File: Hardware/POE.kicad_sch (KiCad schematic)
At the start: 18 parts, among them J1 Conn_01x07_Male, J10 Conn_01x02_Male, J11 Conn_01x02_Male, J2 Conn_01x04_Male, J3 Conn_01x02_Male, J4 Conn_01x02_Male, J5 Conn_01x02_Male, J6 Conn_01x02_Male, J7 Conn_01x08_Male, J9 QWIIC_Stackable

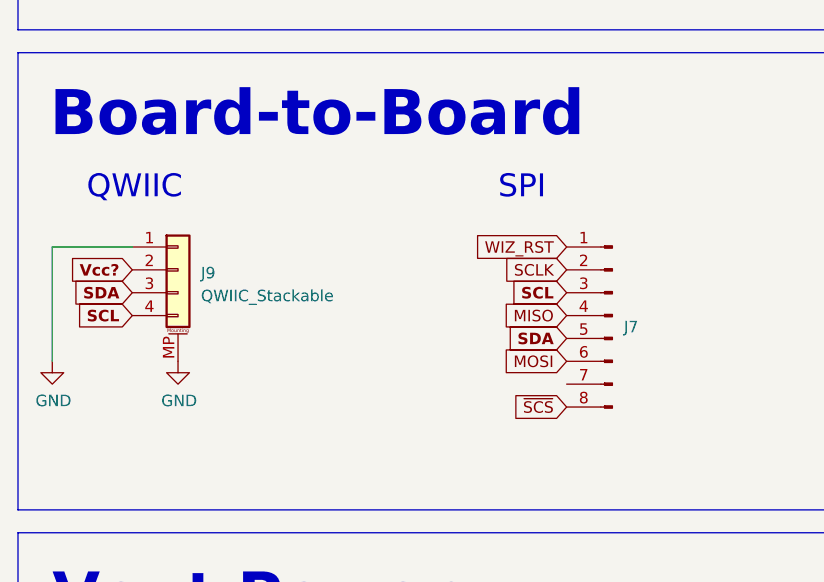
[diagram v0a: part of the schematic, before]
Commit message: Updated POE Board for J7/J9
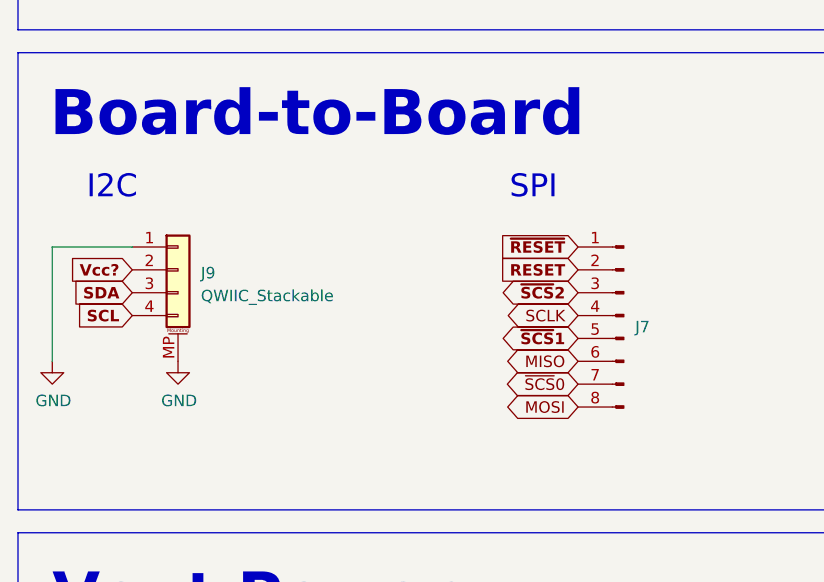
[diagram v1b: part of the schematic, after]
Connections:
- net ~{SCS} is gone; now on net MOSI: J7.8 (Pin_8)
- net MISO: now also J7.6 (Pin_6); no longer J7.4 (Pin_4)
- net MOSI: no longer J7.6 (Pin_6)
- net SCL: no longer J7.3 (Pin_3)
- net SCLK: now also J7.4 (Pin_4); no longer J7.2 (Pin_2)
- net SDA: no longer J7.5 (Pin_5)
- net ~{SCS}0: now reaches J7.7 (Pin_7)
- net WIZ_RST renamed ~{RESET}
- new net RESET: J7.2 (Pin_2)
- new net ~{SCS}1: J7.5 (Pin_5)
- new net ~{SCS}2: J7.3 (Pin_3)
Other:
- note added: "I2C"
- note removed: "QWIIC"
- moved on the sheet: J7
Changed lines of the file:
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@@
   (title_block
     (title "POE")
-    (rev "0.0.0")
+    (rev "0.2.0")
     (company "The Nerd Mage")
     (comment 2 "With help from Austins_Creations")
@@
     (effects (font (size 5 5) (thickness 1) bold) (justify left bottom))
   )
-  (text "QWIIC" (at 21.59 72.39 0)
+  (text "I2C" (at 21.59 72.39 0)
     (effects (font (size 2.54 2.54)) (justify left bottom))
   )
@@
     (effects (font (size 5 5) (thickness 1) bold) (justify left bottom))
   )
-  (text "SPI" (at 67.31 72.39 0)
+  (text "SPI" (at 68.58 72.39 0)
     (effects (font (size 2.54 2.54)) (justify left bottom))
   )
@@
     )
   )
+  (global_label "~{SCS}1" (shape bidirectional) (at 76.2 87.63 180) (fields_autoplaced)
+    (effects (font (size 1.27 1.27) (thickness 0.254) bold) (justify right))
+    (property "Intersheet References" "${INTERSHEET_REFS}" (id 0) (at 68.6979 87.503 0)
+      (effects (font (size 1.27 1.27) (thickness 0.254) bold) (justify right) hide)
+    )
+  )
   (global_label "Vout" (shape input) (at 229.87 143.51 180) (fields_autoplaced)
     (effects (font (size 1.27 1.27)) (justify right))
@@
     )
   )
-  (global_label "MISO" (shape input) (at 74.93 85.09 180) (fields_autoplaced)
-    (effects (font (size 1.27 1.27)) (justify right))
-    (property "Intersheet References" "${INTERSHEET_REFS}" (id 0) (at 67.9207 85.0106 0)
+  (global_label "~{SCS}0" (shape bidirectional) (at 76.2 92.71 180) (fields_autoplaced)
+    (effects (font (size 1.27 1.27)) (justify right))
+    (property "Intersheet References" "${INTERSHEET_REFS}" (id 0) (at 68.8883 92.6306 0)
       (effects (font (size 1.27 1.27)) (justify right) hide)
     )
@@
     )
   )
-  (global_label "SCL" (shape input) (at 74.93 82.55 180) (fields_autoplaced)
-    (effects (font (size 1.27 1.27) (thickness 0.254) bold) (justify right))
-    (property "Intersheet References" "${INTERSHEET_REFS}" (id 0) (at 68.8189 82.423 0)
-      (effects (font (size 1.27 1.27) (thickness 0.254) bold) (justify right) hide)
-    )
-  )
-  (global_label "WIZ_RST" (shape input) (at 74.93 77.47 180) (fields_autoplaced)
-    (effects (font (size 1.27 1.27)) (justify right))
-    (property "Intersheet References" "${INTERSHEET_REFS}" (id 0) (at 64.8364 77.3906 0)
-      (effects (font (size 1.27 1.27)) (justify right) hide)
-    )
-  )
   (global_label "UD-" (shape input) (at 26.67 36.83 180) (fields_autoplaced)
     (effects (font (size 1.27 1.27)) (justify right))
@@
     )
   )
-  (global_label "SCLK" (shape input) (at 74.93 80.01 180) (fields_autoplaced)
-    (effects (font (size 1.27 1.27)) (justify right))
-    (property "Intersheet References" "${INTERSHEET_REFS}" (id 0) (at 67.7393 79.9306 0)
-      (effects (font (size 1.27 1.27)) (justify right) hide)
-    )
-  )
   (global_label "VB2" (shape input) (at 146.05 105.41 180) (fields_autoplaced)
     (effects (font (size 1.27 1.27)) (justify right))
@@
     )
   )
+  (global_label "MISO" (shape bidirectional) (at 76.2 90.17 180) (fields_autoplaced)
+    (effects (font (size 1.27 1.27)) (justify right))
+    (property "Intersheet References" "${INTERSHEET_REFS}" (id 0) (at 69.1907 90.0906 0)
+      (effects (font (size 1.27 1.27)) (justify right) hide)
+    )
+  )
   (global_label "Vin-" (shape input) (at 213.36 146.05 0) (fields_autoplaced)
     (effects (font (size 1.27 1.27)) (justify left))
@@
     )
   )
-  (global_label "~{SCS}" (shape input) (at 74.93 95.25 180) (fields_autoplaced)
-    (effects (font (size 1.27 1.27)) (justify right))
-    (property "Intersheet References" "${INTERSHEET_REFS}" (id 0) (at 68.8279 95.1706 0)
+  (global_label "SCLK" (shape bidirectional) (at 76.2 85.09 180) (fields_autoplaced)
+    (effects (font (size 1.27 1.27)) (justify right))
+    (property "Intersheet References" "${INTERSHEET_REFS}" (id 0) (at 69.0093 85.0106 0)
       (effects (font (size 1.27 1.27)) (justify right) hide)
     )
@@
     )
   )
-  (global_label "MOSI" (shape input) (at 74.93 90.17 180) (fields_autoplaced)
-    (effects (font (size 1.27 1.27)) (justify right))
-    (property "Intersheet References" "${INTERSHEET_REFS}" (id 0) (at 67.9207 90.0906 0)
-      (effects (font (size 1.27 1.27)) (justify right) hide)
-    )
-  )
   (global_label "+3V3" (shape input) (at 83.82 27.94 0) (fields_autoplaced)
     (effects (font (size 1.27 1.27)) (justify left))
@@
     )
   )
+  (global_label "RESET" (shape input) (at 76.2 80.01 180) (fields_autoplaced)
+    (effects (font (size 1.27 1.27) (thickness 0.254) bold) (justify right))
+    (property "Intersheet References" "${INTERSHEET_REFS}" (id 0) (at 67.8513 79.883 0)
+      (effects (font (size 1.27 1.27) (thickness 0.254) bold) (justify right) hide)
+    )
+  )
   (global_label "VB2" (shape input) (at 148.59 54.61 180) (fields_autoplaced)
     (effects (font (size 1.27 1.27)) (justify right))
@@
     )
   )
+  (global_label "~{RESET}" (shape input) (at 76.2 77.47 180) (fields_autoplaced)
+    (effects (font (size 1.27 1.27) (thickness 0.254) bold) (justify right))
+    (property "Intersheet References" "${INTERSHEET_REFS}" (id 0) (at 67.8513 77.343 0)
+      (effects (font (size 1.27 1.27) (thickness 0.254) bold) (justify right) hide)
+    )
+  )
   (global_label "VB1" (shape input) (at 146.05 102.87 180) (fields_autoplaced)
     (effects (font (size 1.27 1.27)) (justify right))
@@
     )
   )
+  (global_label "MOSI" (shape bidirectional) (at 76.2 95.25 180) (fields_autoplaced)
+    (effects (font (size 1.27 1.27)) (justify right))
+    (property "Intersheet References" "${INTERSHEET_REFS}" (id 0) (at 69.1907 95.1706 0)
+      (effects (font (size 1.27 1.27)) (justify right) hide)
+    )
+  )
   (global_label "Vsec" (shape input) (at 53.34 172.72 180) (fields_autoplaced)
     (effects (font (size 1.27 1.27)) (justify right))
@@
     )
   )
+  (global_label "~{SCS}2" (shape bidirectional) (at 76.2 82.55 180) (fields_autoplaced)
+    (effects (font (size 1.27 1.27) (thickness 0.254) bold) (justify right))
+    (property "Intersheet References" "${INTERSHEET_REFS}" (id 0) (at 68.6979 82.423 0)
+      (effects (font (size 1.27 1.27) (thickness 0.254) bold) (justify right) hide)
+    )
+  )
   (global_label "Vin-" (shape input) (at 273.05 146.05 0) (fields_autoplaced)
     (effects (font (size 1.27 1.27)) (justify left))
     (property "Intersheet References" "${INTERSHEET_REFS}" (id 0) (at 279.8779 145.9706 0)
       (effects (font (size 1.27 1.27)) (justify left) hide)
-    )
-  )
-  (global_label "SDA" (shape input) (at 74.93 87.63 180) (fields_autoplaced)
-    (effects (font (size 1.27 1.27) bold) (justify right))
-    (property "Intersheet References" "${INTERSHEET_REFS}" (id 0) (at 68.7584 87.503 0)
-      (effects (font (size 1.27 1.27) bold) (justify right) hide)
     )
   )
@@
     (pin "1")
   )
-  (symbol (lib_id "Connector:Conn_01x08_Male") (at 80.01 85.09 0) (mirror y) (unit 1)
+  (symbol (lib_id "Connector:Conn_01x08_Male") (at 81.28 85.09 0) (mirror y) (unit 1)
     (in_bom yes) (on_board yes) (fields_autoplaced)
-    (property "Reference" "J7" (id 0) (at 81.28 86.3599 0)
+    (property "Reference" "J7" (id 0) (at 82.55 86.3599 0)
       (effects (font (size 1.27 1.27)) (justify right))
     )
-    (property "Value" "Conn_01x08_Male" (id 1) (at 81.28 87.6299 0)
-      (effects (font (size 1.27 1.27)) (justify right) hide)
-    )
-    (property "Footprint" "Tinker:PinHeader_2x04_P1.27mm_Vertical" (id 2) (at 80.01 85.09 0)
-      (effects (font (size 1.27 1.27)) hide)
-    )
-    (property "Datasheet" "~" (id 3) (at 80.01 85.09 0)
-      (effects (font (size 1.27 1.27)) hide)
-    )
-    (property "LCSC" "C2881786 + C2684732" (id 4) (at 80.01 85.09 0)
-      (effects (font (size 1.27 1.27)) hide)
-    )
+    (property "Value" "Conn_01x08_Male" (id 1) (at 82.55 87.6299 0)
+      (effects (font (size 1.27 1.27)) (justify right) hide)
+    )
+    (property "Footprint" "Tinker:PinHeader_2x04_P1.27mm_Vertical" (id 2) (at 81.28 85.09 0)
+      (effects (font (size 1.27 1.27)) hide)
+    )
+    (property "Datasheet" "~" (id 3) (at 81.28 85.09 0)
+      (effects (font (size 1.27 1.27)) hide)
+    )
+    (property "LCSC" "C2881786 + C2684732" (id 4) (at 81.28 85.09 0)
+      (effects (font (size 1.27 1.27)) hide)
+    )
